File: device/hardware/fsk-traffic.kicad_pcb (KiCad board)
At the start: 2 copper layers, 36.7 x 43.4 mm, 40 parts, among them J1 JTAG, J2 USB_C, J3 5268-03AX, J4 5268-03AX, J5 5268-03AX, Q1 MMBT5551, Q2 MMBT5401, Q3 MMBT5551, Q4 MMBT5401, U1 XC6206P332MR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

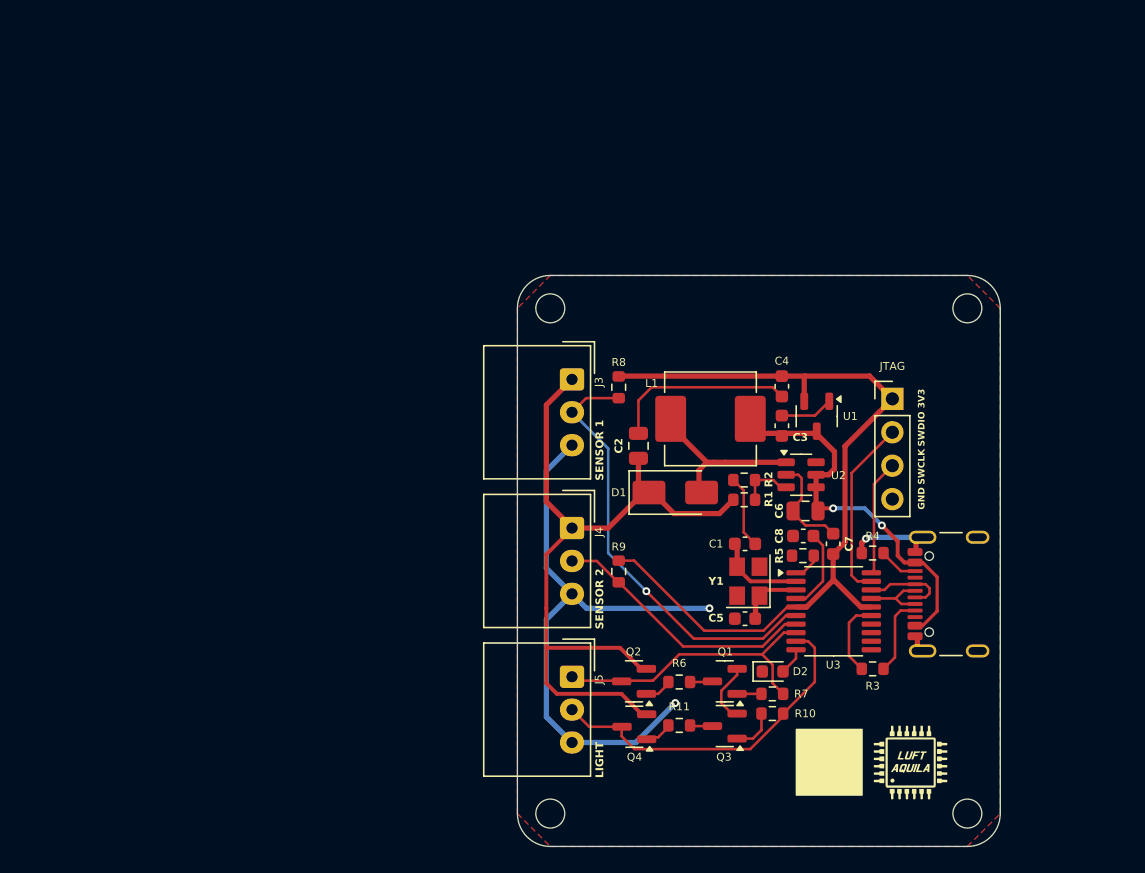
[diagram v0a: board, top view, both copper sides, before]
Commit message: update: PCB v2
fix SSR Hi-side driver and MT3608 layout
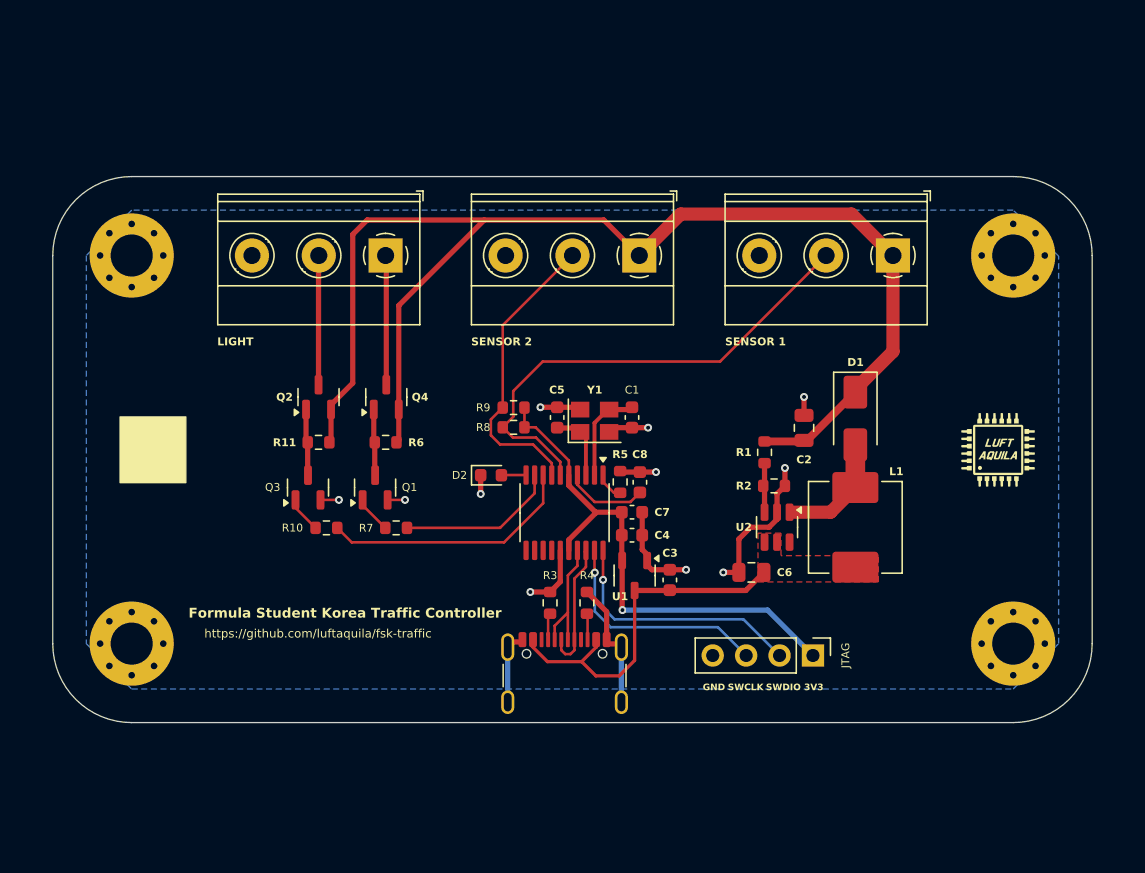
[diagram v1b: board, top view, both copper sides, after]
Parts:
- removed the REF** at (174.2, 132.3)
- removed the REF** at (142.5, 132.3)
- removed the REF** at (142.5, 93.9)
- removed the REF** at (174.2, 93.9)
- added REF**: MountingHole_3.2mm_M3_Pad_Via, MountingHole:MountingHole_3.2mm_M3_Pad_Via, F.Cu at (110.7, 89.9)
- added REF**: MountingHole_3.2mm_M3_Pad_Via, MountingHole:MountingHole_3.2mm_M3_Pad_Via, F.Cu at (177.7, 89.9)
- added REF**: MountingHole_3.2mm_M3_Pad_Via, MountingHole:MountingHole_3.2mm_M3_Pad_Via, F.Cu at (110.7, 119.4)
- added REF**: MountingHole_3.2mm_M3_Pad_Via, MountingHole:MountingHole_3.2mm_M3_Pad_Via, F.Cu at (177.7, 119.4)
- J3, J4, J5: value 5268-03AX -> 2EDGV-5.08-03P; footprint Connector_Molex:Molex_SPOX_5268-03A_1x03_P2.50mm_Horizontal -> TerminalBlock_Phoenix:TerminalBlock_Phoenix_MKDS-1,5-3-5.08_1x03_P5.08mm_Horizontal
- Q2, Q4: value MMBT5401 -> AO3401A
- R11, R6: value 1k -> 10k
- moved R10 36.7 mm to (125.5, 110.6)
- moved Q3 36.5 mm to (124.1, 107.5), turned to 90 degrees
- moved J5 35.0 mm to (130.0, 89.9), turned to 180 degrees
- moved R11 34.9 mm to (124.9, 104.1), turned to 180 degrees
- moved Q2 32.3 mm to (124.9, 100.6), turned to 90 degrees
- moved Q4 31.4 mm to (130.0, 100.6), turned to 90 degrees
- moved R7 31.3 mm to (130.8, 110.6)
- moved J2 31.1 mm to (143.6, 122.8), turned to 0 degrees
- moved Q1 30.4 mm to (129.2, 107.5), turned to 90 degrees
- moved R6 28.8 mm to (130.0, 104.1)
- moved J3 26.1 mm to (168.5, 89.9), turned to 180 degrees
- moved D2 26.1 mm to (138.0, 106.6)
- moved R3 25.0 mm to (142.5, 116.3), turned to -90 degrees
- moved G*** 24.7 mm to (176.6, 104.6)
- moved R4 22.0 mm to (145.3, 116.3), turned to -90 degrees
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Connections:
- J1 pad 2: SWDIO -> SWCLK
- J1 pad 3: SWCLK -> SWDIO
- J5 pad 1: GREEN -> /GN
- J5 pad 2: RED -> /RD
- Q2 pad 1: Net-(Q2-B) -> Net-(Q2-G)
- Q2 pad 3: GREEN -> /RD
- Q3 pad 3: Net-(Q3-C) -> Net-(Q2-G)
- Q4 pad 1: Net-(Q4-B) -> Net-(Q1-C)
- Q4 pad 3: RED -> /GN
- R11 pad 1: Net-(Q4-B) -> 18V
- R11 pad 2: Net-(Q3-C) -> Net-(Q2-G)
- R6 pad 1: Net-(Q2-B) -> Net-(Q1-C)
- R6 pad 2: Net-(Q1-C) -> 18V
- U3 pad 8: GREEN -> RED
- U3 pad 9: RED -> GREEN
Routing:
- net GND: track 96.8 -> 52.9 mm, vias 3 -> 11
- net 18V: track 62.5 -> 101.5 mm
- net +3V3: track 64.0 -> 40.5 mm, vias 0 -> 1
- net SWCLK: track 8.80 -> 19.3 mm, vias 0 -> 1
- net GREEN: track 22.3 -> 12.4 mm
- net /GN: track 0.00 -> 9.85 mm
- net /RD: track 0.00 -> 9.83 mm
- net RED: track 26.6 -> 19.5 mm
- net Net-(Q2-G): track 0.00 -> 5.06 mm
- net Net-(D1-A): track 13.4 -> 8.73 mm
- net USB_DM: track 5.28 -> 9.63 mm
- net SENS1: track 33.5 -> 37.6 mm, vias 1 -> 0
- net SWDIO: track 13.9 -> 17.5 mm, vias 0 -> 1
- net USB_DP: track 6.49 -> 10.1 mm
- net Net-(J2-CC1): track 6.07 -> 2.43 mm
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- added copper zone on F.Cu, net +5V
- added copper zone on B.Cu, net GND
- removed copper zone on F.Cu, net GND
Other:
- board size 36.7 x 43.4 mm -> 79 x 41.5 mm
- board text added: "Formula Student Korea Traffic Controller"
- board text added: "https://github.com/luftaquila/fsk-traffic"

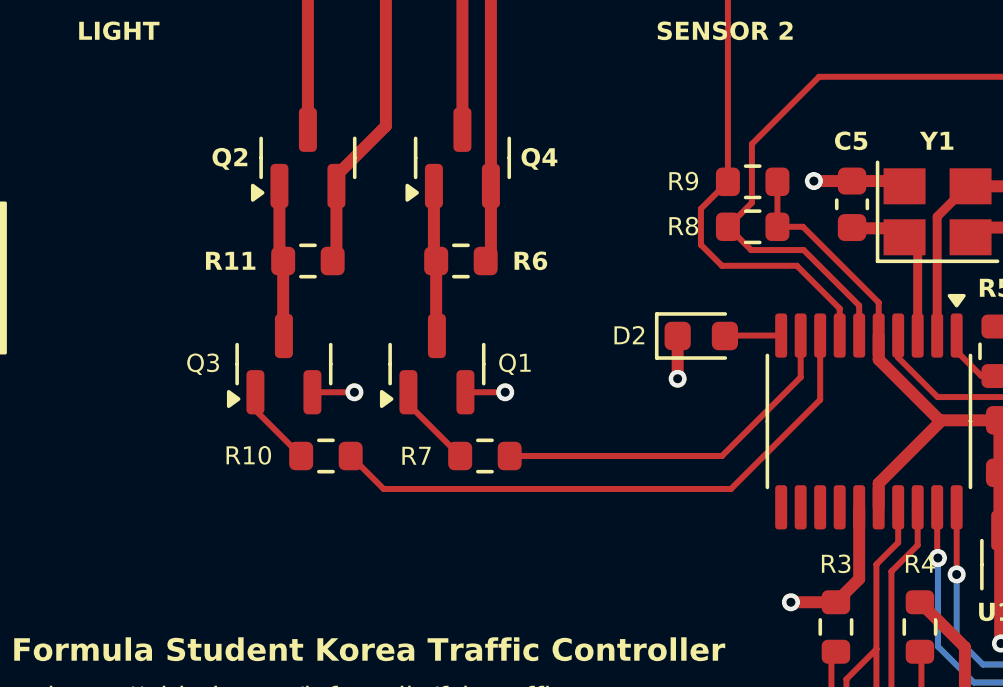
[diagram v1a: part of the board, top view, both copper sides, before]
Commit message: fix: add resistor divider to protect PMOS
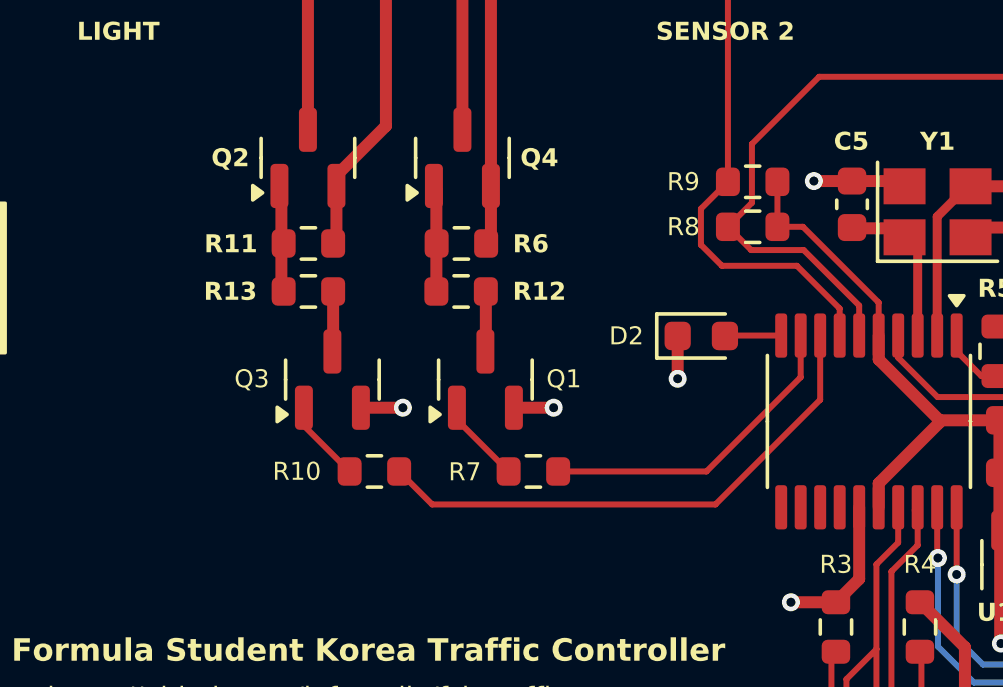
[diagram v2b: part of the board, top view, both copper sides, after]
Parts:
- added R12: 15k, Resistor_SMD:R_0603_1608Metric, F.Cu at (130.0, 105.1)
- added R13: 15k, Resistor_SMD:R_0603_1608Metric, F.Cu at (124.9, 105.1)
- moved Q1 1.70 mm to (130.8, 108.0)
- moved Q3 1.70 mm to (125.7, 108.0)
- moved R10 1.70 mm to (127.1, 111.1)
- moved R7 1.70 mm to (132.4, 111.1)
- moved R11 0.58 mm to (124.9, 103.5)
- moved R6 0.58 mm to (130.0, 103.5)
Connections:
- Q3 pad 3: Net-(Q2-G) -> Net-(Q3-C)
- Q4 pad 1: Net-(Q1-C) -> Net-(Q4-G)
- R6 pad 1: Net-(Q1-C) -> Net-(Q4-G)
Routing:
- net Net-(Q4-G): track 0.00 -> 3.71 mm
- net Net-(Q1-C): track 5.04 -> 2.04 mm
- net Net-(Q3-C): track 0.00 -> 2.05 mm
- net GREEN: track 12.4 -> 10.8 mm
- net Net-(Q2-G): track 5.06 -> 3.53 mm
- net RED: track 19.5 -> 18.1 mm
- net 18V: track 101.5 -> 100.3 mm

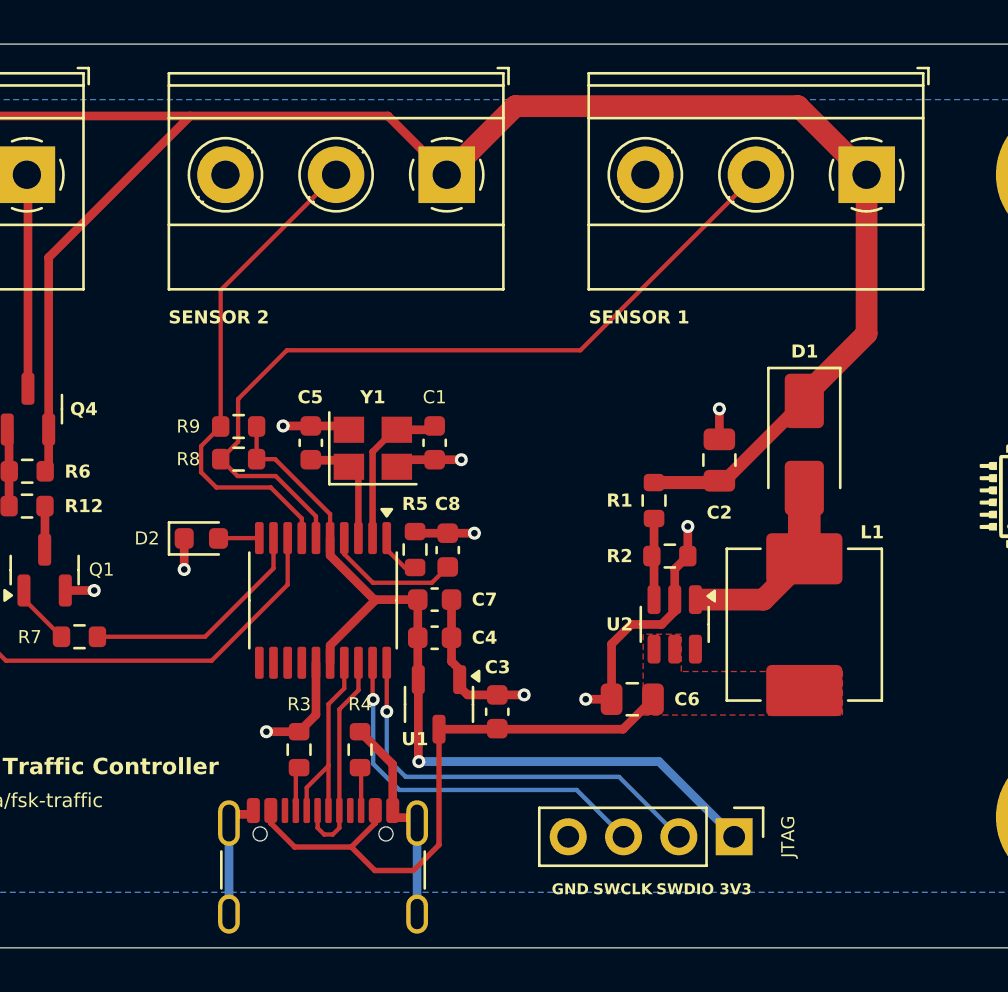
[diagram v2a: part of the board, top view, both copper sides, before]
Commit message: fix: misc pcb bugs
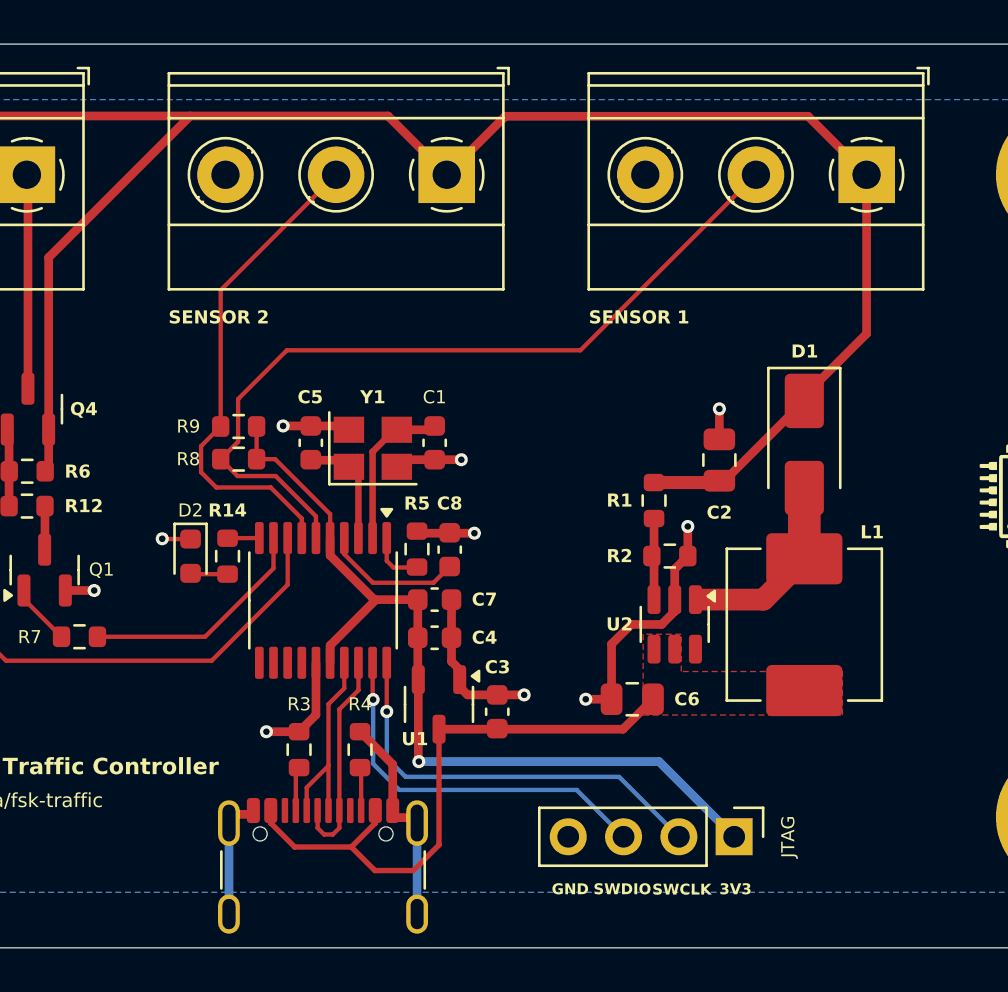
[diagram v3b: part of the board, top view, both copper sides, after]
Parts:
- added R14: 1k, Resistor_SMD:R_0603_1608Metric, F.Cu at (139.2, 107.4)
- moved D2 0.96 mm to (137.5, 107.4), turned to -90 degrees
- moved C8 0.09 mm to (149.4, 107.1)
- moved R5 0.09 mm to (147.9, 107.1)
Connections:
- D2 pad 2: LED -> Net-(D2-A)
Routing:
- net Net-(D2-A): track 0.00 -> 1.72 mm

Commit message: fix: isolation & filter
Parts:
- added C10: 470nF, Capacitor_SMD:C_0603_1608Metric, F.Cu at (143.5, 104.7)
- added C9: 470nF, Capacitor_SMD:C_0603_1608Metric, F.Cu at (140.5, 104.7)
- added R15: 2k, Resistor_SMD:R_0603_1608Metric, F.Cu at (159.8, 89.5)
- added R16: 2k, Resistor_SMD:R_0603_1608Metric, F.Cu at (138.7, 89.5)
- added U4: LTV-817S, Package_DIP:SMDIP-4_W9.53mm, F.Cu at (155.4, 95.6)
- added U5: LTV-817S, Package_DIP:SMDIP-4_W9.53mm, F.Cu at (134.3, 95.6)
- J3, J4, J5: value 2EDGV-5.08-03P -> Molex 5569-04A1; footprint TerminalBlock_Phoenix:TerminalBlock_Phoenix_MKDS-1,5-3-5.08_1x03_P5.08mm_Horizontal -> Connector_Molex:Molex_Mini-Fit_Jr_5569-04A1_2x02_P4.20mm_Horizontal
- R8, R9: value 1k -> 3.3k
- moved J5 9.08 mm to (121.0, 88.6), turned to 0 degrees
- moved J4 7.28 mm to (142.1, 88.6), turned to 0 degrees
- moved J3 5.50 mm to (163.2, 88.6), turned to 0 degrees
- moved R12 4.92 mm to (125.1, 104.9)
- moved R6 4.92 mm to (125.1, 103.3)
- moved Q1 4.91 mm to (125.9, 108.1)
- moved R7 4.91 mm to (127.5, 111.1)
- moved Q4 4.90 mm to (125.2, 100.0)
- moved REF** 4.47 mm to (179.7, 85.9)
- moved REF** 4.45 mm to (108.7, 85.9)
- moved R11 3.96 mm to (121.0, 103.2)
- moved R13 3.96 mm to (121.0, 104.8)
- moved Q2 3.95 mm to (121.0, 99.9)
- moved Q3 3.95 mm to (121.8, 108.0)
- moved R10 3.95 mm to (123.2, 111.1)
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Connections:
- J3 pad 2: SENS1 -> unconnected-(J3-Pin_2-Pad2)
- J3 pad 3: GND -> Net-(J3-Pin_3)
- J4 pad 2: SENS2 -> 18V
- J4 pad 3: GND -> Net-(J4-Pin_3)
- J5 pad 1: /GN -> GND
- J5 pad 2: /RD -> unconnected-(J5-Pin_2-Pad2)
- J5 pad 3: GND -> /RD
- R8 pad 1: +3V3 -> SENS1
- R8 pad 2: SENS1 -> +3V3
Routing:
- net 18V: track 99.9 -> 73.1 mm
- net SENS1: track 37.6 -> 23.7 mm
- net SENS2: track 22.6 -> 11.7 mm
- net Net-(J4-Pin_3): track 0.00 -> 10.5 mm
- net Net-(J3-Pin_3): track 0.00 -> 10.4 mm
- net GND: track 52.8 -> 60.3 mm, vias 11 -> 15
- net GREEN: track 10.8 -> 15.7 mm
- net /GN: track 9.85 -> 5.01 mm
- net /RD: track 9.83 -> 5.01 mm
- net Net-(R16-Pad2): track 0.00 -> 4.09 mm
- net RED: track 18.1 -> 22.0 mm
- net +3V3: track 40.5 -> 44.3 mm, vias 1 -> 3
- net Net-(R15-Pad2): track 0.00 -> 3.34 mm
- net OSC_IN: track 7.16 -> 8.21 mm
- net OSC_OUT: track 5.04 -> 5.73 mm
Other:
- board size 79 x 41.5 mm -> 83 x 45.5 mm

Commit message: fix: missing pcb 18V wiring
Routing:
- net 18V: track 73.1 -> 78.2 mm, vias 0 -> 2
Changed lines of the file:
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@@
+	)
+	(segment
+		(start 125.8375 103.2625)
+		(end 125.05 104.05)
+		(width 0.2)
+		(layer "F.Cu")
+		(net 14)
 	)
 	(segment
@@
 		(end 126.075 103.34058)
 		(width 0.4)
+		(layer "F.Cu")
+		(net 14)
+	)
+	(segment
+		(start 125.9125 103.2625)
+		(end 125.8375 103.2625)
+		(width 0.2)
 		(layer "F.Cu")
 		(net 14)
@@
 	)
 	(segment
+		(start 122.575 104.05)
+		(end 121.775 103.25)
+		(width 0.2)
+		(layer "F.Cu")
+		(net 14)
+	)
+	(segment
 		(start 126.1375 100.8875)
 		(end 126.1375 97.9625)
@@
 		(net 14)
 	)
+	(via
+		(at 122.575 104.05)
+		(size 0.6)
+		(drill 0.3)
+		(layers "F.Cu" "B.Cu")
+		(net 14)
+	)
+	(via
+		(at 125.05 104.05)
+		(size 0.6)
+		(drill 0.3)
+		(layers "F.Cu" "B.Cu")
+		(net 14)
+	)
+	(segment
+		(start 125.05 104.05)
+		(end 122.575 104.05)
+		(width 0.2)
+		(layer "B.Cu")
+		(net 14)
+	)
+	(segment
+		(start 122.575 104.05)
+		(end 122.8 104.05)
+		(width 0.2)
+		(layer "B.Cu")
+		(net 14)
+	)
